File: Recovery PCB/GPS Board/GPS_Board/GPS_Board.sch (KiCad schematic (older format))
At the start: 15 parts, among them J1 XT30-M, J2 XT30-M, U1 Teensy4.1

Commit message: Created netlist
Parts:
- gave numbers to parts that had none: 8
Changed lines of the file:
@@
 	4000 2100 4300 2100
 $Comp
-L power:+3.3V #PWR?
+L power:+3.3V #PWR0104
 U 1 1 625F178F
 P 5550 3800
-F 0 "#PWR?" H 5550 3650 50  0001 C CNN
+F 0 "#PWR0104" H 5550 3650 50  0001 C CNN
 F 1 "+3.3V" V 5565 3928 50  0000 L CNN
 F 2 "" H 5550 3800 50  0001 C CNN
@@
 	1525 2500 1800 2500
 $Comp
-L power:+3.3V #PWR?
+L power:+3.3V #PWR0108
 U 1 1 625CE6B8
 P 5275 1225
-F 0 "#PWR?" H 5275 1075 50  0001 C CNN
+F 0 "#PWR0108" H 5275 1075 50  0001 C CNN
 F 1 "+3.3V" V 5325 1300 50  0000 C CNN
 F 2 "" H 5275 1225 50  0001 C CNN
@@
 XBEE_SLEEP
 $Comp
-L power:+3.3V #PWR?
+L power:+3.3V #PWR0110
 U 1 1 625E340B
 P 4000 1600
-F 0 "#PWR?" H 4000 1450 50  0001 C CNN
+F 0 "#PWR0110" H 4000 1450 50  0001 C CNN
 F 1 "+3.3V" V 4015 1728 50  0000 L CNN
 F 2 "" H 4000 1600 50  0001 C CNN
@@
 XBEE_SLEEP
 $Comp
-L GPS_Board:D24V22F5_VoltageRegulator U?
+L GPS_Board:D24V22F5_VoltageRegulator U2
 U 1 1 6257FB96
 P 9300 1900
-F 0 "U?" H 9578 1946 50  0000 L CNN
+F 0 "U2" H 9578 1946 50  0000 L CNN
 F 1 "D24V22F5_VoltageRegulator" H 9578 1855 50  0000 L CNN
 F 2 "GPS Board:D24V22F5_VoltageRegulator" H 9750 3100 50  0001 C CNN
@@
 	8950 1800 8575 1800
 $Comp
-L power:GND #PWR?
+L power:GND #PWR0111
 U 1 1 62587171
 P 6975 1325
-F 0 "#PWR?" H 6975 1075 50  0001 C CNN
+F 0 "#PWR0111" H 6975 1075 50  0001 C CNN
 F 1 "GND" H 6980 1152 50  0000 C CNN
 F 2 "" H 6975 1325 50  0001 C CNN
@@
 $EndComp
 $Comp
-L power:+5V #PWR?
+L power:+5V #PWR0112
 U 1 1 62588B60
 P 8950 2100
-F 0 "#PWR?" H 8950 1950 50  0001 C CNN
+F 0 "#PWR0112" H 8950 1950 50  0001 C CNN
 F 1 "+5V" V 8965 2228 50  0000 L CNN
 F 2 "" H 8950 2100 50  0001 C CNN
@@
 $EndComp
 $Comp
-L power:GND #PWR?
+L power:GND #PWR0113
 U 1 1 62589874
 P 8950 1900
-F 0 "#PWR?" H 8950 1650 50  0001 C CNN
+F 0 "#PWR0113" H 8950 1650 50  0001 C CNN
 F 1 "GND" V 8955 1772 50  0000 R CNN
 F 2 "" H 8950 1900 50  0001 C CNN
@@
 $EndComp
 $Comp
-L power:GND #PWR?
+L power:GND #PWR0114
 U 1 1 6258A3E2
 P 8950 2000
-F 0 "#PWR?" H 8950 1750 50  0001 C CNN
+F 0 "#PWR0114" H 8950 1750 50  0001 C CNN
 F 1 "GND" V 8955 1872 50  0000 R CNN
 F 2 "" H 8950 2000 50  0001 C CNN
@@
 $EndComp
 $Comp
-L GPS_Board:LD1117v33 U?
+L GPS_Board:LD1117v33 U3
 U 1 1 625AB452
 P 9300 2675
-F 0 "U?" H 9290 3020 50  0000 C CNN
+F 0 "U3" H 9290 3020 50  0000 C CNN
 F 1 "LD1117v33" H 9290 2929 50  0000 C CNN
 F 2 "Package_TO_SOT_THT:TO-220-3_Horizontal_TabDown" H 9290 2905 50  0001 C CNN
@@
 	8575 2675 8940 2675
 $Comp
-L power:GND #PWR?
+L power:GND #PWR0115
 U 1 1 625C6B48
 P 9640 2765
-F 0 "#PWR?" H 9640 2515 50  0001 C CNN
+F 0 "#PWR0115" H 9640 2515 50  0001 C CNN
 F 1 "GND" V 9645 2637 50  0000 R CNN
 F 2 "" H 9640 2765 50  0001 C CNN
@@
 GPS_RX
 $Comp
-L power:+3.3V #PWR?
+L power:+3.3V #PWR0116
 U 1 1 625EA16C
 P 2750 4850
-F 0 "#PWR?" H 2750 4700 50  0001 C CNN
+F 0 "#PWR0116" H 2750 4700 50  0001 C CNN
 F 1 "+3.3V" H 2765 5023 50  0000 C CNN
 F 2 "" H 2750 4850 50  0001 C CNN
@@
 $EndComp
 $Comp
-L power:GND #PWR?
+L power:GND #PWR0117
 U 1 1 625EB8C1
 P 1800 4550
-F 0 "#PWR?" H 1800 4300 50  0001 C CNN
+F 0 "#PWR0117" H 1800 4300 50  0001 C CNN
 F 1 "GND" V 1805 4422 50  0000 R CNN
 F 2 "" H 1800 4550 50  0001 C CNN
@@
 $EndComp
 $Comp
-L power:GND #PWR?
+L power:GND #PWR0118
 U 1 1 625EC4CE
 P 1800 4450
-F 0 "#PWR?" H 1800 4200 50  0001 C CNN
+F 0 "#PWR0118" H 1800 4200 50  0001 C CNN
 F 1 "GND" V 1805 4322 50  0000 R CNN
 F 2 "" H 1800 4450 50  0001 C CNN
@@
 $EndComp
 $Comp
-L power:+5V #PWR?
+L power:+5V #PWR0119
 U 1 1 625ECDBB
 P 1800 4150
-F 0 "#PWR?" H 1800 4000 50  0001 C CNN
+F 0 "#PWR0119" H 1800 4000 50  0001 C CNN
 F 1 "+5V" V 1815 4278 50  0000 L CNN
 F 2 "" H 1800 4150 50  0001 C CNN
@@
 $EndComp
 $Comp
-L power:+3.3V #PWR?
+L power:+3.3V #PWR0120
 U 1 1 625EDBA6
 P 1800 2800
-F 0 "#PWR?" H 1800 2650 50  0001 C CNN
+F 0 "#PWR0120" H 1800 2650 50  0001 C CNN
 F 1 "+3.3V" V 1815 2928 50  0000 L CNN
 F 2 "" H 1800 2800 50  0001 C CNN
@@
 $EndComp
 $Comp
-L power:GND #PWR?
+L power:GND #PWR0121
 U 1 1 625EF2C8
 P 4000 4050
-F 0 "#PWR?" H 4000 3800 50  0001 C CNN
+F 0 "#PWR0121" H 4000 3800 50  0001 C CNN
 F 1 "GND" V 4005 3922 50  0000 R CNN
 F 2 "" H 4000 4050 50  0001 C CNN
@@
 $EndComp
 $Comp
-L Connector:TestPoint TP?
+L Connector:TestPoint TP8
 U 1 1 625F3DB9
 P 5625 3950
-F 0 "TP?" V 5525 4300 50  0000 C CNN
+F 0 "TP8" V 5525 4300 50  0000 C CNN
 F 1 "TestPoint" V 5625 4350 50  0000 C CNN
 F 2 "" H 5825 3950 50  0001 C CNN
@@
 $EndComp
 $Comp
-L Connector:TestPoint TP?
+L Connector:TestPoint TP7
 U 1 1 625F9755
 P 9655 2451
-F 0 "TP?" V 9609 2639 50  0000 L CNN
+F 0 "TP7" V 9609 2639 50  0000 L CNN
 F 1 "TestPoint" V 9700 2639 50  0000 L CNN
 F 2 "" H 9855 2451 50  0001 C CNN
@@
 Connection ~ 8950 2100
 $Comp
-L Connector:TestPoint TP?
+L Connector:TestPoint TP6
 U 1 1 625FCCAB
 P 8875 2225
-F 0 "TP?" V 8750 2225 50  0000 C CNN
+F 0 "TP6" V 8750 2225 50  0000 C CNN
 F 1 "TestPoint" V 8825 2150 50  0000 C CNN
 F 2 "" H 9075 2225 50  0001 C CNN
@@
 	7100 1325 7225 1325
 $Comp
-L Connector:TestPoint TP?
+L Connector:TestPoint TP4
 U 1 1 62600FE9
 P 7025 1250
-F 0 "TP?" V 7220 1322 50  0000 C CNN
+F 0 "TP4" V 7220 1322 50  0000 C CNN
 F 1 "TestPoint" V 7129 1322 50  0000 C CNN
 F 2 "" H 7225 1250 50  0001 C CNN
@@
 Connection ~ 5425 1225
 $Comp
-L Connector:TestPoint TP?
+L Connector:TestPoint TP3
 U 1 1 62601ADB
 P 5325 1075
-F 0 "TP?" V 5520 1147 50  0000 C CNN
+F 0 "TP3" V 5520 1147 50  0000 C CNN
 F 1 "TestPoint" V 5429 1147 50  0000 C CNN
 F 2 "" H 5525 1075 50  0001 C CNN
@@
 	5325 1075 5425 1075
 $Comp
-L Connector:TestPoint TP?
+L Connector:TestPoint TP5
 U 1 1 626043C8
 P 8350 1650
-F 0 "TP?" H 8400 1850 50  0000 L CNN
+F 0 "TP5" H 8400 1850 50  0000 L CNN
 F 1 "TestPoint" H 8400 1750 50  0000 L CNN
 F 2 "" H 8550 1650 50  0001 C CNN
@@
 	9640 2451 9655 2451
 $Comp
-L power:+3.3V #PWR?
+L power:+3.3V #PWR0122
 U 1 1 625C7E59
 P 9640 2580
-F 0 "#PWR?" H 9640 2430 50  0001 C CNN
+F 0 "#PWR0122" H 9640 2430 50  0001 C CNN
 F 1 "+3.3V" V 9655 2708 50  0000 L CNN
 F 2 "" H 9640 2580 50  0001 C CNN

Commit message: Fixed power routing
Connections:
- net +3V3: no longer U1.15 (3V3), U1.46 (3V3), U1.51 (3V3)
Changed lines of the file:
@@
 $EndDescr
-$Comp
-L GPS_Board-rescue:Teensy4.1-teensy U1
-U 1 1 61A899BD
-P 2900 3550
-F 0 "U1" H 2900 6115 50  0000 C CNN
-F 1 "Teensy4.1" H 2900 6024 50  0000 C CNN
-F 2 "GPS Board:Teensy41" H 2500 3950 50  0001 C CNN
-F 3 "" H 2500 3950 50  0001 C CNN
-	1    2900 3550
-	1    0    0    -1
-$EndComp
 $Comp
 L GPS_Board:XT30-M J1
@@
 Wire Wire Line
 	2950 4850 2950 5125
-Connection ~ 2900 4850
 $Comp
 L power:GND #PWR0109
@@
 Text Label 4300 3700 2    39   ~ 0
 XBEE_SLEEP
-$Comp
-L power:+3.3V #PWR0110
-U 1 1 625E340B
-P 4000 1600
-F 0 "#PWR0110" H 4000 1450 50  0001 C CNN
-F 1 "+3.3V" V 4015 1728 50  0000 L CNN
-F 2 "" H 4000 1600 50  0001 C CNN
-F 3 "" H 4000 1600 50  0001 C CNN
-	1    4000 1600
-	0    1    1    0
-$EndComp
 Text Label 6675 2125 2    39   ~ 0
 XBee_MOSI
@@
 $EndComp
 Wire Wire Line
-	1800 3300 1525 3300
-Wire Wire Line
-	1800 3400 1525 3400
-Wire Wire Line
 	6275 1525 6575 1525
 Wire Wire Line
@@
 Text Label 5150 1425 0    39   ~ 0
 XBEE_RX
-Text Label 1525 3300 0    39   ~ 0
-XBEE_TX
-Text Label 1525 3400 0    39   ~ 0
-XBEE_RX
 Wire Wire Line
 	1800 1500 1525 1500
@@
 Text Label 1525 1600 0    39   ~ 0
 GPS_RX
-$Comp
-L power:+3.3V #PWR0116
-U 1 1 625EA16C
-P 2750 4850
-F 0 "#PWR0116" H 2750 4700 50  0001 C CNN
-F 1 "+3.3V" H 2765 5023 50  0000 C CNN
-F 2 "" H 2750 4850 50  0001 C CNN
-F 3 "" H 2750 4850 50  0001 C CNN
-	1    2750 4850
-	-1   0    0    1
-$EndComp
 $Comp
 L power:GND #PWR0117
@@
 $EndComp
 $Comp
-L power:+3.3V #PWR0120
-U 1 1 625EDBA6
-P 1800 2800
-F 0 "#PWR0120" H 1800 2650 50  0001 C CNN
-F 1 "+3.3V" V 1815 2928 50  0000 L CNN
-F 2 "" H 1800 2800 50  0001 C CNN
-F 3 "" H 1800 2800 50  0001 C CNN
-	1    1800 2800
-	0    -1   -1   0
-$EndComp
-$Comp
 L power:GND #PWR0121
 U 1 1 625EF2C8
@@
 $EndComp
 Connection ~ 9640 2580
+Connection ~ 2900 4850
+Text Label 1525 3400 0    39   ~ 0
+XBEE_RX
+Text Label 1525 3300 0    39   ~ 0
+XBEE_TX
+Wire Wire Line
+	1800 3400 1525 3400
+Wire Wire Line
+	1800 3300 1525 3300
+$Comp
+L GPS_Board-rescue:Teensy4.1-teensy U1
+U 1 1 61A899BD
+P 2900 3550
+F 0 "U1" H 2900 6115 50  0000 C CNN
+F 1 "Teensy4.1" H 2900 6024 50  0000 C CNN
+F 2 "GPS Board:Teensy41" H 2500 3950 50  0001 C CNN
+F 3 "" H 2500 3950 50  0001 C CNN
+	1    2900 3550
+	1    0    0    -1
+$EndComp
 $EndSCHEMATC

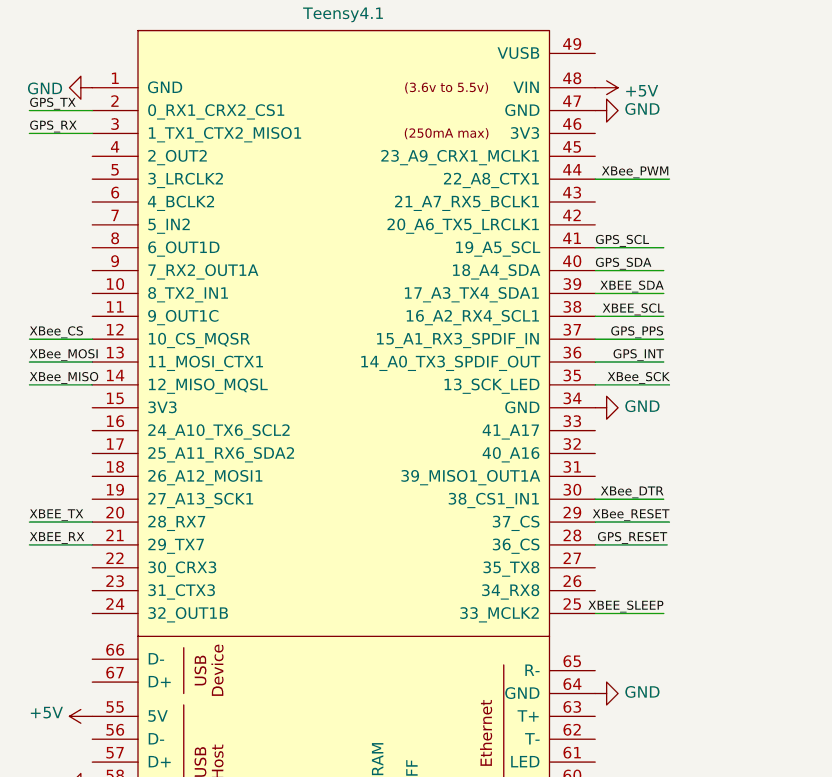
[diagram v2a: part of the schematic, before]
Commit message: Routed all traces and removed vias
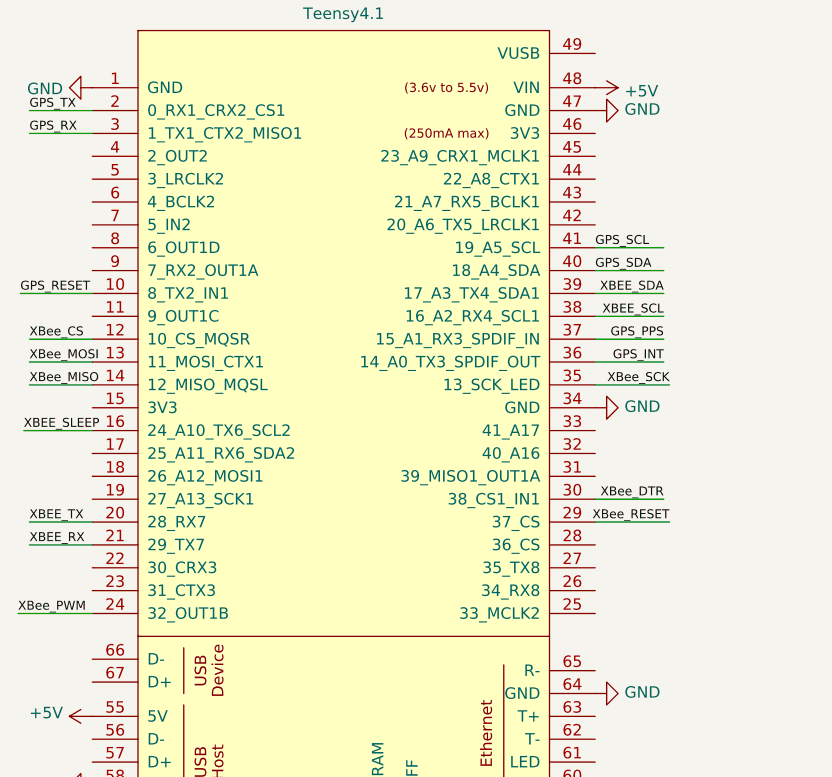
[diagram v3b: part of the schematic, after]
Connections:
- net GPS_RESET: now also U1.10 (8_TX2_IN1); no longer U1.28 (36_CS)
- net XBEE_SLEEP: now also U1.16 (24_A10_TX6_SCL2); no longer U1.25 (33_MCLK2)
- net XBee_PWM: now also U1.24 (32_OUT1B); no longer U1.44 (22_A8_CTX1)
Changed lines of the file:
@@
 	0    -1   -1   0
 $EndComp
-Text Label 4315 3400 2    39   ~ 0
+Text Label 1485 2300 0    39   ~ 0
 GPS_RESET
 Wire Wire Line
-	4000 3400 4315 3400
+	1800 2300 1485 2300
 Text Label 7400 3800 2    39   ~ 0
 GPS_RESET
@@
 XBee_PWM
 Wire Wire Line
-	4000 1800 4325 1800
-Text Label 4325 1800 2    39   ~ 0
+	1800 3700 1475 3700
+Text Label 1475 3700 0    39   ~ 0
 XBee_PWM
 Text Label 5150 2025 0    39   ~ 0
@@
 XBee_DTR
 Wire Wire Line
-	4000 3700 4300 3700
-Text Label 4300 3700 2    39   ~ 0
+	1800 2900 1500 2900
+Text Label 1500 2900 0    39   ~ 0
 XBEE_SLEEP
 Text Label 6675 2125 2    39   ~ 0

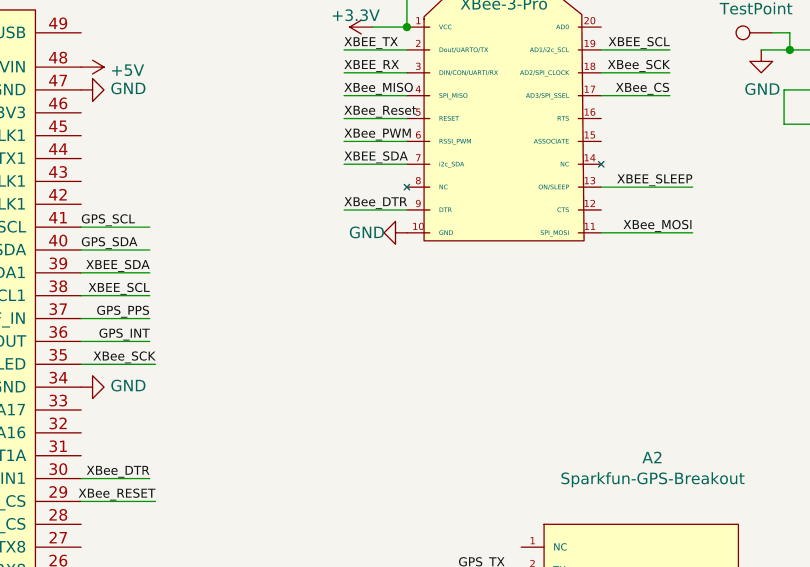
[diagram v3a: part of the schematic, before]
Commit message: Added test points
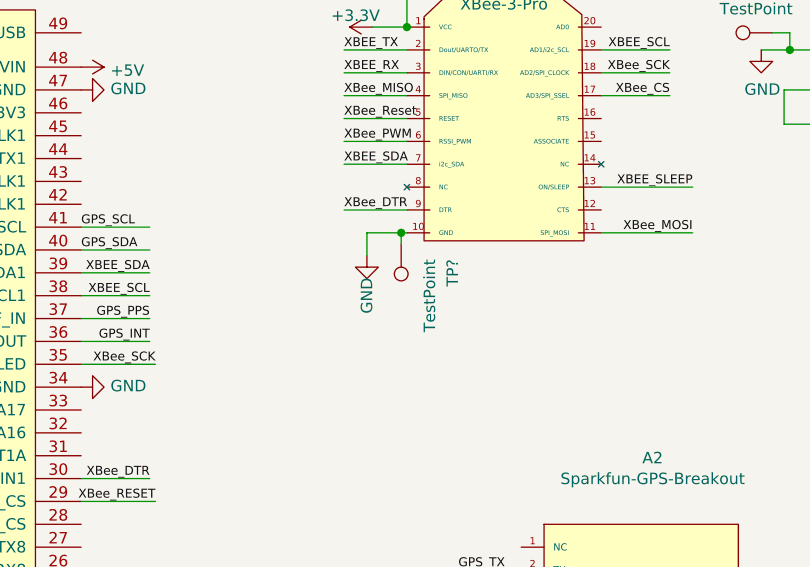
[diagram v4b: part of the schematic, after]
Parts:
- added TP?: TestPoint, TestPoint:TestPoint_Pad_D2.0mm, symbol Connector:TestPoint
- TP1, TP2: footprint TestPoint:TestPoint_Pad_D1.5mm -> TestPoint:TestPoint_Pad_D2.0mm
- TP3, TP4, TP5, TP6, TP7: footprint (none) -> TestPoint:TestPoint_Pad_D2.0mm
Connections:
- net GND: now also TP?.1
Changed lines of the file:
@@
 L power:GND #PWR0106
 U 1 1 61ACAD1F
-P 5425 2125
-F 0 "#PWR0106" H 5425 1875 50  0001 C CNN
-F 1 "GND" V 5425 1950 50  0000 C CNN
-F 2 "" H 5425 2125 50  0001 C CNN
-F 3 "" H 5425 2125 50  0001 C CNN
-	1    5425 2125
-	0    1    1    0
+P 5250 2225
+F 0 "#PWR0106" H 5250 1975 50  0001 C CNN
+F 1 "GND" V 5250 2050 50  0000 C CNN
+F 2 "" H 5250 2225 50  0001 C CNN
+F 3 "" H 5250 2225 50  0001 C CNN
+	1    5250 2225
+	1    0    0    -1
 $EndComp
 $Comp
@@
 F 0 "TP2" H 2842 4876 50  0000 R CNN
 F 1 "TestPoint" H 2842 4967 50  0000 R CNN
-F 2 "TestPoint:TestPoint_Pad_D1.5mm" H 3100 4850 50  0001 C CNN
+F 2 "TestPoint:TestPoint_Pad_D2.0mm" H 3100 4850 50  0001 C CNN
 F 3 "~" H 3100 4850 50  0001 C CNN
 	1    2900 4850
@@
 F 0 "TP1" H 2900 4900 50  0000 R CNN
 F 1 "TestPoint" H 3000 4975 50  0000 R CNN
-F 2 "TestPoint:TestPoint_Pad_D1.5mm" H 2800 4850 50  0001 C CNN
+F 2 "TestPoint:TestPoint_Pad_D2.0mm" H 2800 4850 50  0001 C CNN
 F 3 "~" H 2800 4850 50  0001 C CNN
 	1    2600 4850
@@
 F 0 "TP7" V 9609 2639 50  0000 L CNN
 F 1 "TestPoint" V 9700 2639 50  0000 L CNN
-F 2 "" H 9855 2451 50  0001 C CNN
+F 2 "TestPoint:TestPoint_Pad_D2.0mm" H 9855 2451 50  0001 C CNN
 F 3 "~" H 9855 2451 50  0001 C CNN
 	1    9655 2451
@@
 F 0 "TP6" V 8750 2225 50  0000 C CNN
 F 1 "TestPoint" V 8825 2150 50  0000 C CNN
-F 2 "" H 9075 2225 50  0001 C CNN
+F 2 "TestPoint:TestPoint_Pad_D2.0mm" H 9075 2225 50  0001 C CNN
 F 3 "~" H 9075 2225 50  0001 C CNN
 	1    8875 2225
@@
 F 0 "TP4" V 7220 1322 50  0000 C CNN
 F 1 "TestPoint" V 7129 1322 50  0000 C CNN
-F 2 "" H 7225 1250 50  0001 C CNN
+F 2 "TestPoint:TestPoint_Pad_D2.0mm" H 7225 1250 50  0001 C CNN
 F 3 "~" H 7225 1250 50  0001 C CNN
 	1    7025 1250
@@
 F 0 "TP3" V 5520 1147 50  0000 C CNN
 F 1 "TestPoint" V 5429 1147 50  0000 C CNN
-F 2 "" H 5525 1075 50  0001 C CNN
+F 2 "TestPoint:TestPoint_Pad_D2.0mm" H 5525 1075 50  0001 C CNN
 F 3 "~" H 5525 1075 50  0001 C CNN
 	1    5325 1075
@@
 F 0 "TP5" H 8400 1850 50  0000 L CNN
 F 1 "TestPoint" H 8400 1750 50  0000 L CNN
-F 2 "" H 8550 1650 50  0001 C CNN
+F 2 "TestPoint:TestPoint_Pad_D2.0mm" H 8550 1650 50  0001 C CNN
 F 3 "~" H 8550 1650 50  0001 C CNN
 	1    8350 1650
@@
 	1    0    0    -1
 $EndComp
+$Comp
+L Connector:TestPoint TP?
+U 1 1 625C34C1
+P 5400 2175
+F 0 "TP?" V 5175 2300 50  0000 C CNN
+F 1 "TestPoint" V 5275 2400 50  0000 C CNN
+F 2 "TestPoint:TestPoint_Pad_D2.0mm" H 5600 2175 50  0001 C CNN
+F 3 "~" H 5600 2175 50  0001 C CNN
+	1    5400 2175
+	-1   0    0    1
+$EndComp
+Wire Wire Line
+	5250 2225 5250 2125
+Wire Wire Line
+	5250 2125 5400 2125
+Wire Wire Line
+	5400 2175 5400 2125
+Connection ~ 5400 2125
+Wire Wire Line
+	5400 2125 5425 2125
 $EndSCHEMATC
